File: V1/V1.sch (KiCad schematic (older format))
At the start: 42 parts, among them J1 acheronSymbols_TYPE-C-31-M12_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, SW1 SW_Push, U1 ATmega32U4-AU, Y1 16MHz

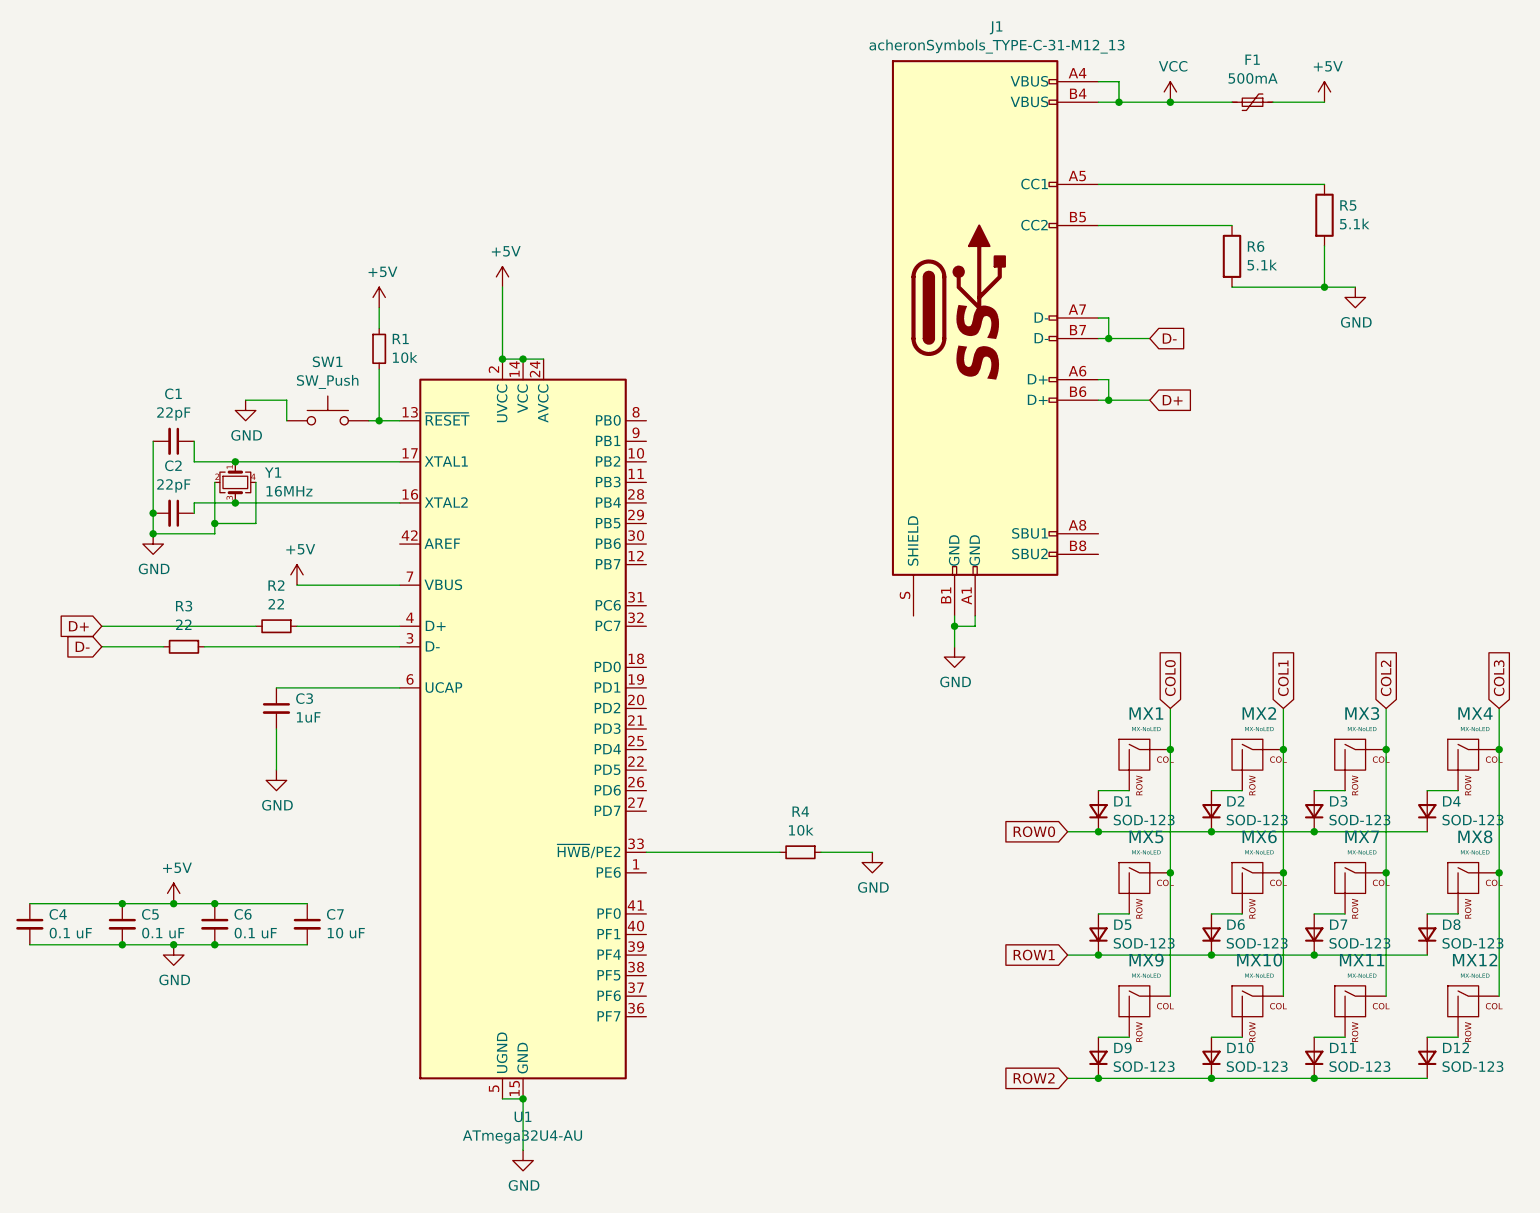
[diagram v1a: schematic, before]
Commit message: PCB and Routing done. Adjusted Type C connectors further
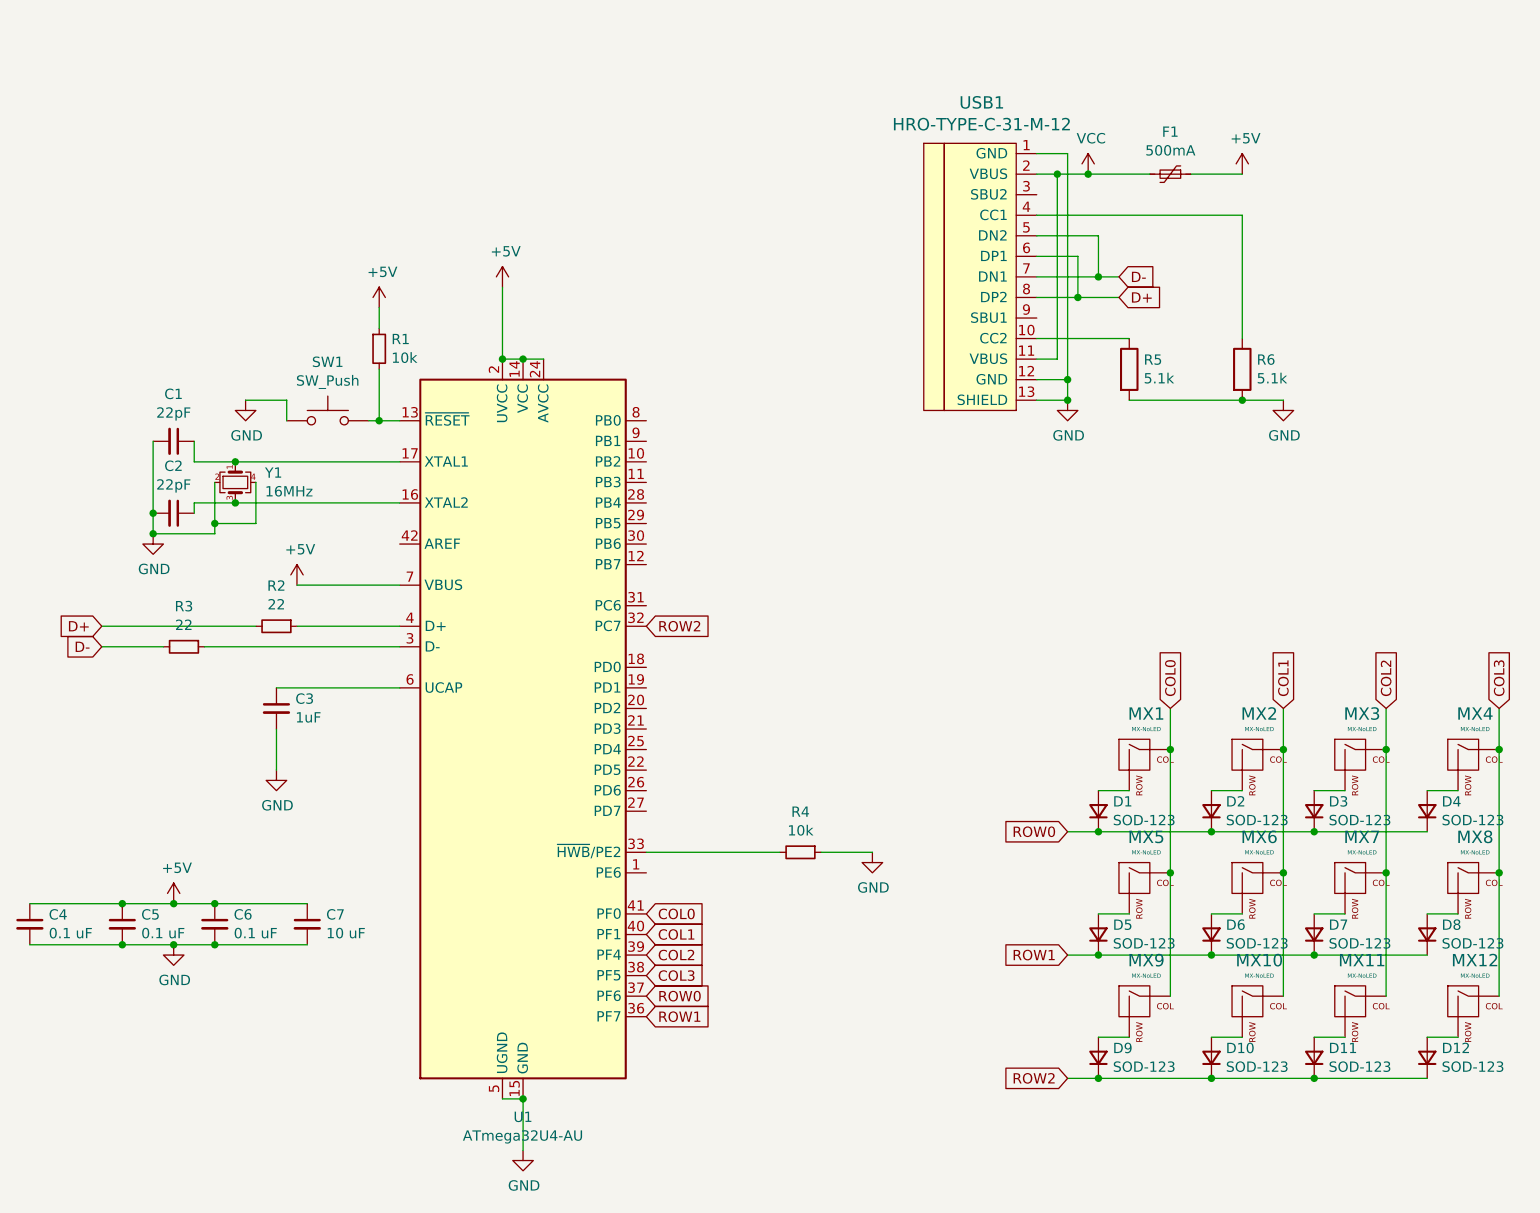
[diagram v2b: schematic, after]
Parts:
- removed J1: acheronSymbols_TYPE-C-31-M12_13, acheronConnectors:TYPE-C-31-M-12, symbol Unified-Daughterboard-cache:acheronSymbols_TYPE-C-31-M12_13
- added USB1: HRO-TYPE-C-31-M-12, Type-C:HRO-TYPE-C-31-M-12-Assembly, symbol Type-C:HRO-TYPE-C-31-M-12
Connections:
- net COL0: now also U1.41 (PF0)
- net COL1: now also U1.40 (PF1)
- net COL2: now also U1.39 (PF4)
- net COL3: now also U1.38 (PF5)
- net D+: now also USB1.6 (DP1), USB1.8 (DP2)
- net D-: now also USB1.5 (DN2), USB1.7 (DN1)
- net GND: now also USB1.1 (GND), USB1.12 (GND), USB1.13 (SHIELD)
- net ROW0: now also U1.37 (PF6)
- net ROW1: now also U1.36 (PF7)
- net ROW2: now also U1.32 (PC7)
- net VCC: now also USB1.11 (VBUS), USB1.2 (VBUS)
- net at R5.1: now also USB1.10 (CC2)
- net at R6.1: now also USB1.4 (CC1)
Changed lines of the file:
@@
 Text GLabel 10200 3900 1    50   Input ~ 0
 COL3
+Wire Wire Line
+	8250 1600 7950 1600
+Wire Wire Line
+	8250 1800 8250 1600
+Wire Wire Line
+	7950 1700 8150 1700
+Wire Wire Line
+	8150 1900 7950 1900
+Wire Wire Line
+	8150 1700 8150 1900
+Wire Wire Line
+	7950 1800 8250 1800
+Wire Wire Line
+	8250 1800 8350 1800
+Connection ~ 8250 1800
+Wire Wire Line
+	8150 1900 8350 1900
+Connection ~ 8150 1900
+Text GLabel 8350 1800 2    50   Input ~ 0
+D-
+Text GLabel 8350 1900 2    50   Input ~ 0
+D+
+Wire Wire Line
+	7950 1300 8050 1300
+Wire Wire Line
+	8050 1300 8050 2200
 $Comp
-L Unified-Daughterboard-cache:acheronSymbols_TYPE-C-31-M12_13 J1
-U 1 1 61804EB1
-P 7650 2000
-F 0 "J1" H 7757 3417 50  0000 C CNN
-F 1 "acheronSymbols_TYPE-C-31-M12_13" H 7757 3326 50  0000 C CNN
-F 2 "acheronConnectors:TYPE-C-31-M-12" V 7150 2050 50  0001 C CNN
-F 3 "" H 7850 2050 50  0001 C CNN
-	1    7650 2000
+L Device:Polyfuse_Small F1
+U 1 1 618ADFB5
+P 8600 1300
+F 0 "F1" V 8395 1300 50  0000 C CNN
+F 1 "500mA" V 8486 1300 50  0000 C CNN
+F 2 "Fuse:Fuse_1206_3216Metric" H 8650 1100 50  0001 L CNN
+F 3 "~" H 8600 1300 50  0001 C CNN
+	1    8600 1300
+	0    1    1    0
+$EndComp
+Wire Wire Line
+	8700 1300 8950 1300
+$Comp
+L power:VCC #PWR0111
+U 1 1 618B5D12
+P 8200 1300
+F 0 "#PWR0111" H 8200 1150 50  0001 C CNN
+F 1 "VCC" H 8215 1473 50  0000 C CNN
+F 2 "" H 8200 1300 50  0001 C CNN
+F 3 "" H 8200 1300 50  0001 C CNN
+	1    8200 1300
 	1    0    0    -1
 $EndComp
 Wire Wire Line
-	8250 950  8350 950
-Wire Wire Line
-	8250 850  8350 850
-Wire Wire Line
-	8350 850  8350 950
-Connection ~ 8350 950
-Wire Wire Line
-	8350 950  8600 950
-$Comp
-L power:VCC #PWR0111
-U 1 1 6183E869
-P 8600 950
-F 0 "#PWR0111" H 8600 800 50  0001 C CNN
-F 1 "VCC" H 8615 1123 50  0000 C CNN
-F 2 "" H 8600 950 50  0001 C CNN
-F 3 "" H 8600 950 50  0001 C CNN
-	1    8600 950
-	1    0    0    -1
-$EndComp
-$Comp
-L Device:Polyfuse_Small F1
-U 1 1 6183FB82
-P 9000 950
-F 0 "F1" V 8795 950 50  0000 C CNN
-F 1 "500mA" V 8886 950 50  0000 C CNN
-F 2 "Fuse:Fuse_1206_3216Metric" H 9050 750 50  0001 L CNN
-F 3 "~" H 9000 950 50  0001 C CNN
-	1    9000 950
-	0    1    1    0
-$EndComp
-Wire Wire Line
-	8600 950  8900 950
-Connection ~ 8600 950
-Wire Wire Line
-	9100 950  9350 950
+	8200 1300 8500 1300
+Connection ~ 8200 1300
 $Comp
 L power:+5V #PWR0112
-U 1 1 618452D0
-P 9350 950
-F 0 "#PWR0112" H 9350 800 50  0001 C CNN
-F 1 "+5V" H 9365 1123 50  0000 C CNN
-F 2 "" H 9350 950 50  0001 C CNN
-F 3 "" H 9350 950 50  0001 C CNN
-	1    9350 950
+U 1 1 618B9BA0
+P 8950 1300
+F 0 "#PWR0112" H 8950 1150 50  0001 C CNN
+F 1 "+5V" H 8965 1473 50  0000 C CNN
+F 2 "" H 8950 1300 50  0001 C CNN
+F 3 "" H 8950 1300 50  0001 C CNN
+	1    8950 1300
 	1    0    0    -1
 $EndComp
 Wire Wire Line
-	8250 2100 8300 2100
+	7950 1200 8100 1200
 Wire Wire Line
-	8250 2000 8300 2000
-Wire Wire Line
-	8300 2000 8300 2100
-Connection ~ 8300 2100
-Wire Wire Line
-	8300 2100 8500 2100
-Wire Wire Line
-	8250 2400 8300 2400
-Wire Wire Line
-	8250 2300 8300 2300
-Wire Wire Line
-	8300 2300 8300 2400
-Connection ~ 8300 2400
-Wire Wire Line
-	8300 2400 8500 2400
-Wire Wire Line
-	7550 3450 7550 3500
-Wire Wire Line
-	7650 3450 7650 3500
-Wire Wire Line
-	7650 3500 7550 3500
-Connection ~ 7550 3500
-Wire Wire Line
-	7550 3500 7550 3600
+	7950 2300 8100 2300
 $Comp
 L power:GND #PWR0113
-U 1 1 618653CC
-P 7550 3600
-F 0 "#PWR0113" H 7550 3350 50  0001 C CNN
-F 1 "GND" H 7555 3427 50  0000 C CNN
-F 2 "" H 7550 3600 50  0001 C CNN
-F 3 "" H 7550 3600 50  0001 C CNN
-	1    7550 3600
+U 1 1 618C3AD0
+P 8100 2400
+F 0 "#PWR0113" H 8100 2150 50  0001 C CNN
+F 1 "GND" H 8105 2227 50  0000 C CNN
+F 2 "" H 8100 2400 50  0001 C CNN
+F 3 "" H 8100 2400 50  0001 C CNN
+	1    8100 2400
 	1    0    0    -1
 $EndComp
-Text GLabel 8500 2100 2    50   Input ~ 0
-D-
-Text GLabel 8500 2400 2    50   Input ~ 0
-D+
 Wire Wire Line
-	8250 1350 9350 1350
+	8100 1200 8100 2300
 Wire Wire Line
-	8250 1550 8900 1550
+	8050 1300 8200 1300
+$Comp
+L Type-C:HRO-TYPE-C-31-M-12 USB1
+U 1 1 618918E4
+P 7850 1750
+F 0 "USB1" H 7683 2547 60  0000 C CNN
+F 1 "HRO-TYPE-C-31-M-12" H 7683 2441 60  0000 C CNN
+F 2 "Type-C:HRO-TYPE-C-31-M-12-Assembly" H 7850 1750 60  0001 C CNN
+F 3 "" H 7850 1750 60  0001 C CNN
+	1    7850 1750
+	1    0    0    -1
+$EndComp
+Wire Wire Line
+	7950 2200 8050 2200
 $Comp
 L Device:R R6
-U 1 1 6186EFA0
-P 8900 1700
-F 0 "R6" H 8970 1746 50  0000 L CNN
-F 1 "5.1k" H 8970 1655 50  0000 L CNN
-F 2 "Resistor_SMD:R_0805_2012Metric" V 8830 1700 50  0001 C CNN
-F 3 "~" H 8900 1700 50  0001 C CNN
-	1    8900 1700
+U 1 1 618EF802
+P 8950 2250
+F 0 "R6" H 9020 2296 50  0000 L CNN
+F 1 "5.1k" H 9020 2205 50  0000 L CNN
+F 2 "Resistor_SMD:R_0805_2012Metric" V 8880 2250 50  0001 C CNN
+F 3 "~" H 8950 2250 50  0001 C CNN
+	1    8950 2250
 	1    0    0    -1
 $EndComp
 $Comp
 L Device:R R5
-U 1 1 6187320B
-P 9350 1500
-F 0 "R5" H 9420 1546 50  0000 L CNN
-F 1 "5.1k" H 9420 1455 50  0000 L CNN
-F 2 "Resistor_SMD:R_0805_2012Metric" V 9280 1500 50  0001 C CNN
-F 3 "~" H 9350 1500 50  0001 C CNN
-	1    9350 1500
+U 1 1 618F264E
+P 8400 2250
+F 0 "R5" H 8470 2296 50  0000 L CNN
+F 1 "5.1k" H 8470 2205 50  0000 L CNN
+F 2 "Resistor_SMD:R_0805_2012Metric" V 8330 2250 50  0001 C CNN
+F 3 "~" H 8400 2250 50  0001 C CNN
+	1    8400 2250
 	1    0    0    -1
 $EndComp
 Wire Wire Line
-	8900 1850 9350 1850
+	8400 2400 8950 2400
+Connection ~ 8950 2400
 Wire Wire Line
-	9350 1650 9350 1850
-Connection ~ 9350 1850
-Wire Wire Line
-	9350 1850 9500 1850
+	8950 2400 9150 2400
 $Comp
 L power:GND #PWR0114
-U 1 1 6187AC07
-P 9500 1850
-F 0 "#PWR0114" H 9500 1600 50  0001 C CNN
-F 1 "GND" H 9505 1677 50  0000 C CNN
-F 2 "" H 9500 1850 50  0001 C CNN
-F 3 "" H 9500 1850 50  0001 C CNN
-	1    9500 1850
+U 1 1 618FCE62
+P 9150 2400
+F 0 "#PWR0114" H 9150 2150 50  0001 C CNN
+F 1 "GND" H 9155 2227 50  0000 C CNN
+F 2 "" H 9150 2400 50  0001 C CNN
+F 3 "" H 9150 2400 50  0001 C CNN
+	1    9150 2400
 	1    0    0    -1
 $EndComp
+Connection ~ 8050 1300
+Wire Wire Line
+	7950 2100 8400 2100
+Wire Wire Line
+	8950 2100 8950 1500
+Wire Wire Line
+	8950 1500 7950 1500
+Wire Wire Line
+	7950 2400 8100 2400
+Wire Wire Line
+	8100 2300 8100 2400
+Connection ~ 8100 2300
+Connection ~ 8100 2400
+Text GLabel 6050 4900 2    50   Input ~ 0
+COL0
+Text GLabel 6050 5000 2    50   Input ~ 0
+COL1
+Text GLabel 6050 5100 2    50   Input ~ 0
+COL2
+Text GLabel 6050 5200 2    50   Input ~ 0
+COL3
+Text GLabel 6050 5300 2    50   Input ~ 0
+ROW0
+Text GLabel 6050 5400 2    50   Input ~ 0
+ROW1
+Text GLabel 6050 3500 2    50   Input ~ 0
+ROW2
 $EndSCHEMATC
